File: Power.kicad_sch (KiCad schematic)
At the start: 31 parts, among them J1 S2B-PH-K-S, Q2 SSM3J35MFV, Q3 SSM3K16FV, U6 TPS629203DRL, U9 TPS629206DRLR

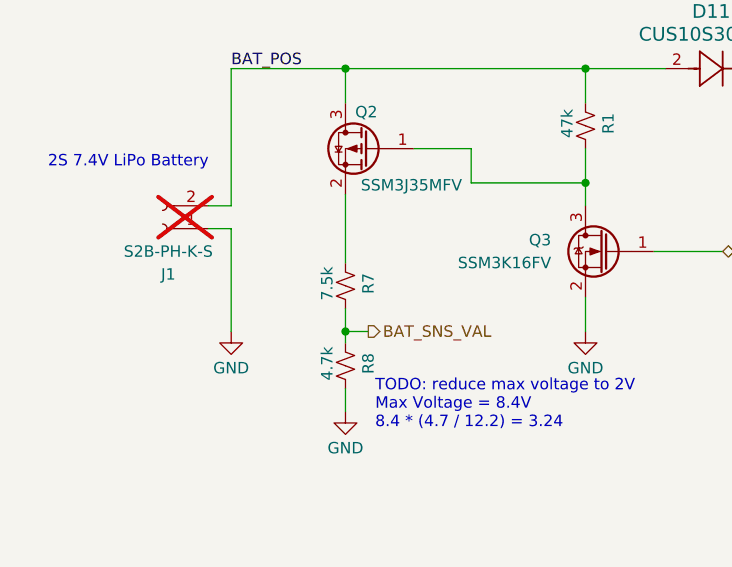
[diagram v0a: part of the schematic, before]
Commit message: rev2 precheck DRC clean
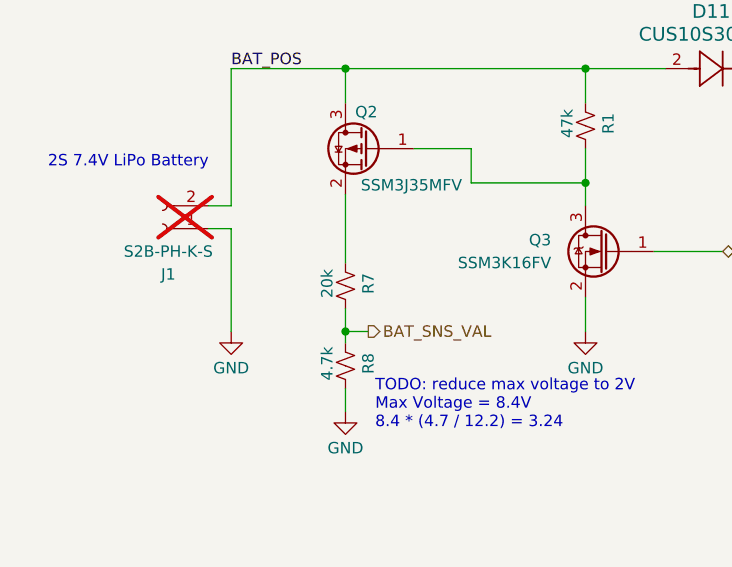
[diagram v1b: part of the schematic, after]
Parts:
- R7: value 7.5k -> 20k; Distributor Prt # 311-7.50KLRCT-ND -> 311-20.0KLRCT-ND; Manuf Prt # RC0402FR-077K5L -> RC0402FR-0720KL
- TP11, TP14, TP15, TP7, TP8: footprint TestPoint:TestPoint_Pad_D1.0mm -> TestPoint:TestPoint_THTPad_1.0x1.0mm_Drill0.5mm
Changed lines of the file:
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@@
 			)
 		)
-		(property "Footprint" "TestPoint:TestPoint_Pad_D1.0mm"
+		(property "Footprint" "TestPoint:TestPoint_THTPad_1.0x1.0mm_Drill0.5mm"
 			(at 105.41 81.28 0)
 			(effects
@@
 			)
 		)
-		(property "Footprint" "TestPoint:TestPoint_Pad_D1.0mm"
+		(property "Footprint" "TestPoint:TestPoint_THTPad_1.0x1.0mm_Drill0.5mm"
 			(at 267.97 41.91 0)
 			(effects
@@
 			)
 		)
-		(property "Footprint" "TestPoint:TestPoint_Pad_D1.0mm"
+		(property "Footprint" "TestPoint:TestPoint_THTPad_1.0x1.0mm_Drill0.5mm"
 			(at 204.47 107.95 0)
 			(effects
@@
 			)
 		)
-		(property "Footprint" "TestPoint:TestPoint_Pad_D1.0mm"
+		(property "Footprint" "TestPoint:TestPoint_THTPad_1.0x1.0mm_Drill0.5mm"
 			(at 96.52 81.28 0)
 			(effects
@@
 			)
 		)
-		(property "Footprint" "TestPoint:TestPoint_Pad_D1.0mm"
+		(property "Footprint" "TestPoint:TestPoint_THTPad_1.0x1.0mm_Drill0.5mm"
 			(at 248.92 97.79 0)
 			(effects
@@
 			)
 		)
-		(property "Value" "7.5k"
+		(property "Value" "20k"
 			(at 51.308 103.886 90)
 			(effects
@@
 			)
 		)
-		(property "Description" "RES 7.5K OHM 1% 1/16W 0402"
+		(property "Description" "RES 20K OHM 1% 1/16W 0402"
 			(at 53.34 104.14 0)
 			(effects
@@
 			)
 		)
-		(property "Distributor Prt #" "311-7.50KLRCT-ND"
+		(property "Distributor Prt #" "311-20.0KLRCT-ND"
 			(at 53.34 104.14 0)
 			(effects
@@
 			)
 		)
-		(property "Manuf Prt #" "RC0402FR-077K5L"
+		(property "Manuf Prt #" "RC0402FR-0720KL"
 			(at 53.34 104.14 0)
 			(effects

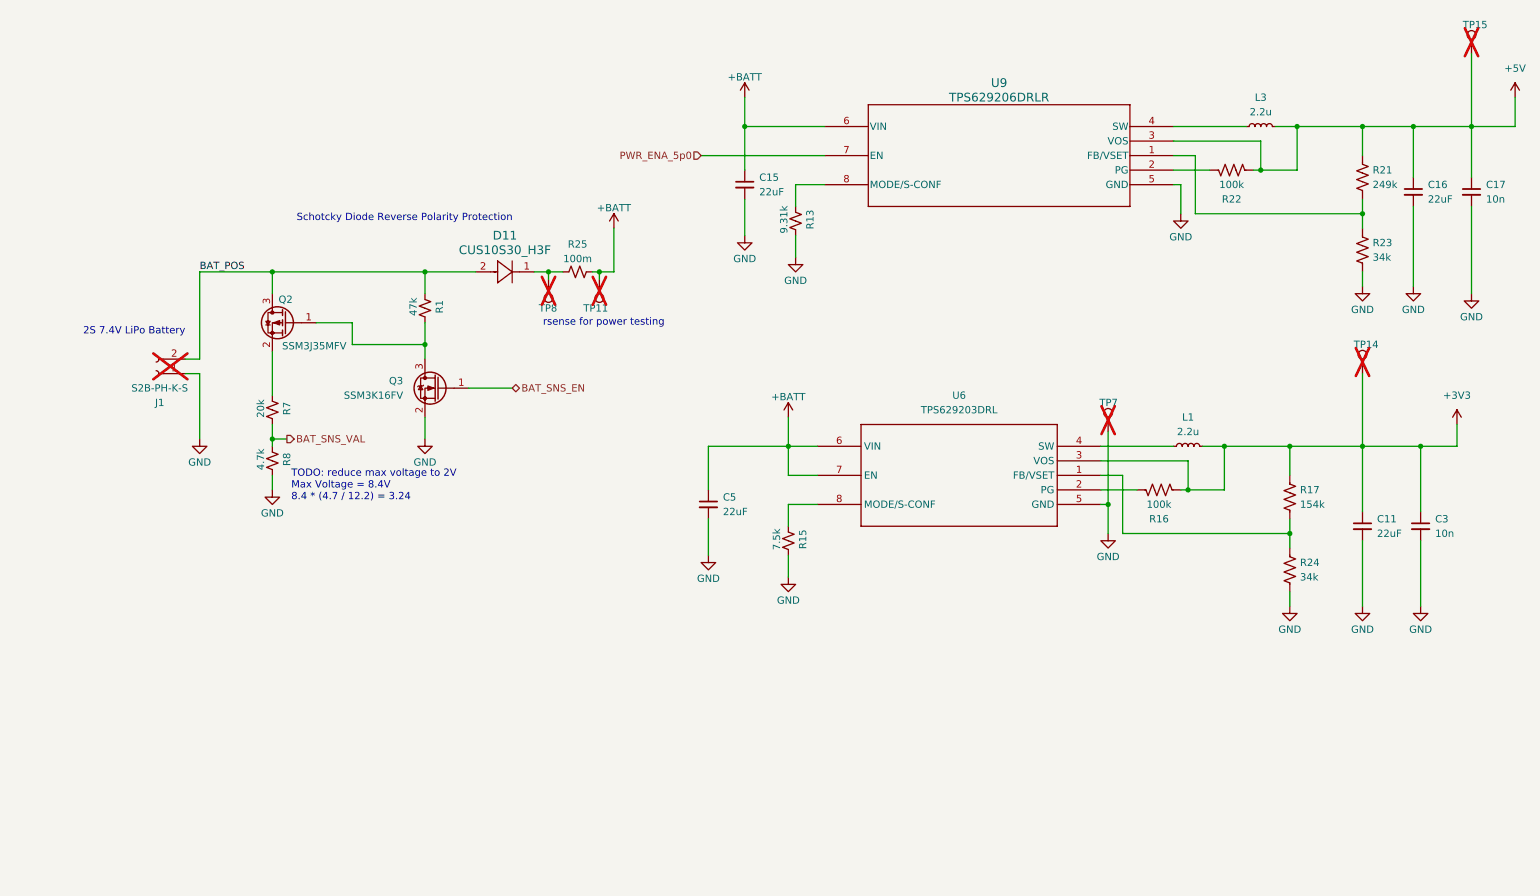
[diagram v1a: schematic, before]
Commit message: updated schematic for pwr savings
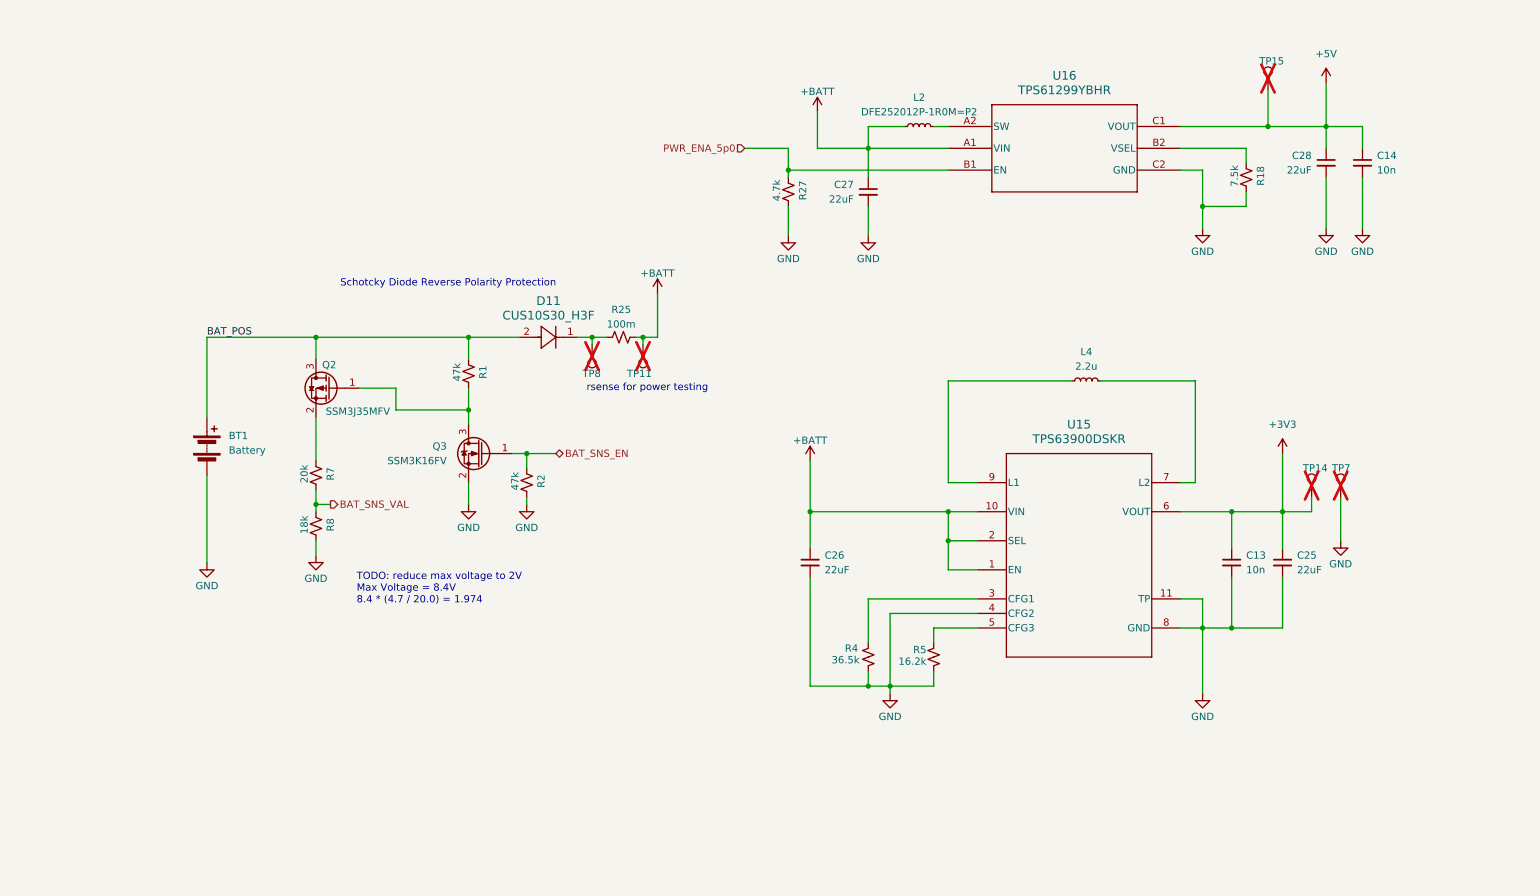
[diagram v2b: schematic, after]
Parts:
- removed C11, C15, C16, C5: 22uF, Capacitor_SMD:C_0805_2012Metric, symbol Device:C_Small
- removed C17, C3: 10n, Capacitor_SMD:C_0201_0603Metric, symbol Device:C_Small
- removed J1: S2B-PH-K-S, SproutSenseFootprints:CONN_S2B-PH-K-S_JST, symbol Connector:Conn_01x02_Socket
- removed L1, L3: 2.2u, SproutSenseFootprints:IND_VLS3012CX-2R2M-1, symbol Device:L_Small
- removed R13: 9.31k, Resistor_SMD:R_0402_1005Metric, symbol Device:R_Small_US
- removed R15: 7.5k, Resistor_SMD:R_0402_1005Metric, symbol Device:R_Small_US
- removed R16, R22: 100k, Resistor_SMD:R_0402_1005Metric, symbol Device:R_US
- removed R17: 154k, Resistor_SMD:R_0402_1005Metric, symbol Device:R_US
- removed R21: 249k, Resistor_SMD:R_0402_1005Metric, symbol Device:R_US
- removed R23, R24: 34k, Resistor_SMD:R_0402_1005Metric, symbol Device:R_US
- removed U6: TPS629203DRL, SproutSenseFootprints:SOT5X3-8_DRL_TEX, symbol SproutSense:TPS629203DRL
- removed U9: TPS629206DRLR, SproutSenseFootprints:SOT5X3-8_DRL_TEX, symbol SproutSense:TPS629206DRLR
- added BT1: Battery, SproutSenseFootprints:BatteryHolder_21700, symbol Device:Battery
- added C13, C14: 10n, Capacitor_SMD:C_0201_0603Metric, symbol Device:C_Small
- added C25, C26, C27, C28: 22uF, Capacitor_SMD:C_0805_2012Metric, symbol Device:C_Small
- added L2: DFE252012P-1R0M=P2, SproutSenseFootprints:DFE252012P-1R0M=P2, symbol Device:L_Small
- added L4: 2.2u, SproutSenseFootprints:IND_VLS3012CX-2R2M-1, symbol Device:L_Small
- added R18: 7.5k, Resistor_SMD:R_0402_1005Metric, symbol Device:R_Small_US
- added R2: 47k, Resistor_SMD:R_0402_1005Metric, symbol Device:R_Small_US
- added R27: 4.7k, Resistor_SMD:R_0402_1005Metric, symbol Device:R_Small_US
- added R4: 36.5k, Resistor_SMD:R_0805_2012Metric, symbol Device:R_Small_US
- added R5: 16.2k, Resistor_SMD:R_0805_2012Metric, symbol Device:R_Small_US
- added U15: TPS63900DSKR, SproutSenseFootprints:DSK0010A, symbol SproutSense:TPS63900DSKR
- added U16: TPS61299YBHR, SproutSenseFootprints:DSBGA6_YBH_TEX, symbol SproutSense:TPS61299YBHR
- R8: value 4.7k -> 18k; Distributor Prt # 311-4.7KJRCT-ND -> A130370TR-ND; Manuf Prt # RC0402JR-074K7L -> CRGP0402F18K
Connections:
- net +3V3: now also C13.1, C25.1, U15.6 (VOUT)
- net +5V: now also C14.1, C28.1, U16.C1 (VOUT)
- net +BATT: now also C26.1, C27.1, L2.1, U15.1 (EN), U15.10 (VIN), U15.2 (SEL), U16.A1 (VIN)
- net BAT_POS: now also BT1.1 (+)
- net BAT_SNS_EN: now also R2.2
- net GND: now also BT1.2 (-), C13.2, C14.2, C25.2, C26.2, C27.2, C28.2, R18.1, R2.1, R27.1, R4.2, R5.2, U15.11 (TP), U15.4 (CFG2), U15.8 (GND), U16.C2 (GND)
- net PWR_ENA_5p0: now also R27.2, U16.B1 (EN)
- new net: R4.1, U15.3 (CFG1)
- new net: L2.2, U16.A2 (SW)
- new net: R5.1, U15.5 (CFG3)
- new net: L4.2, U15.7 (L2)
- new net: L4.1, U15.9 (L1)
- new net: R18.2, U16.B2 (VSEL)
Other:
- note added: "TODO: reduce max voltage to 2V Max Voltage = 8.4V 8.4 * (4.7 / 20.0) = 1.974"
- note removed: "2S 7.4V LiPo Battery"
- note removed: "TODO: reduce max voltage to 2V Max Voltage = 8.4V 8.4 * (4.7 / 12.2) = 3.24"
- title: SproutSyncProto-A-01 -> SproutSyncProto-A-02
- moved on the sheet: D11, Q2, Q3, R1, R25, R7, R8, TP11, TP14, TP7, TP8

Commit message: updated pcb for pwr savings
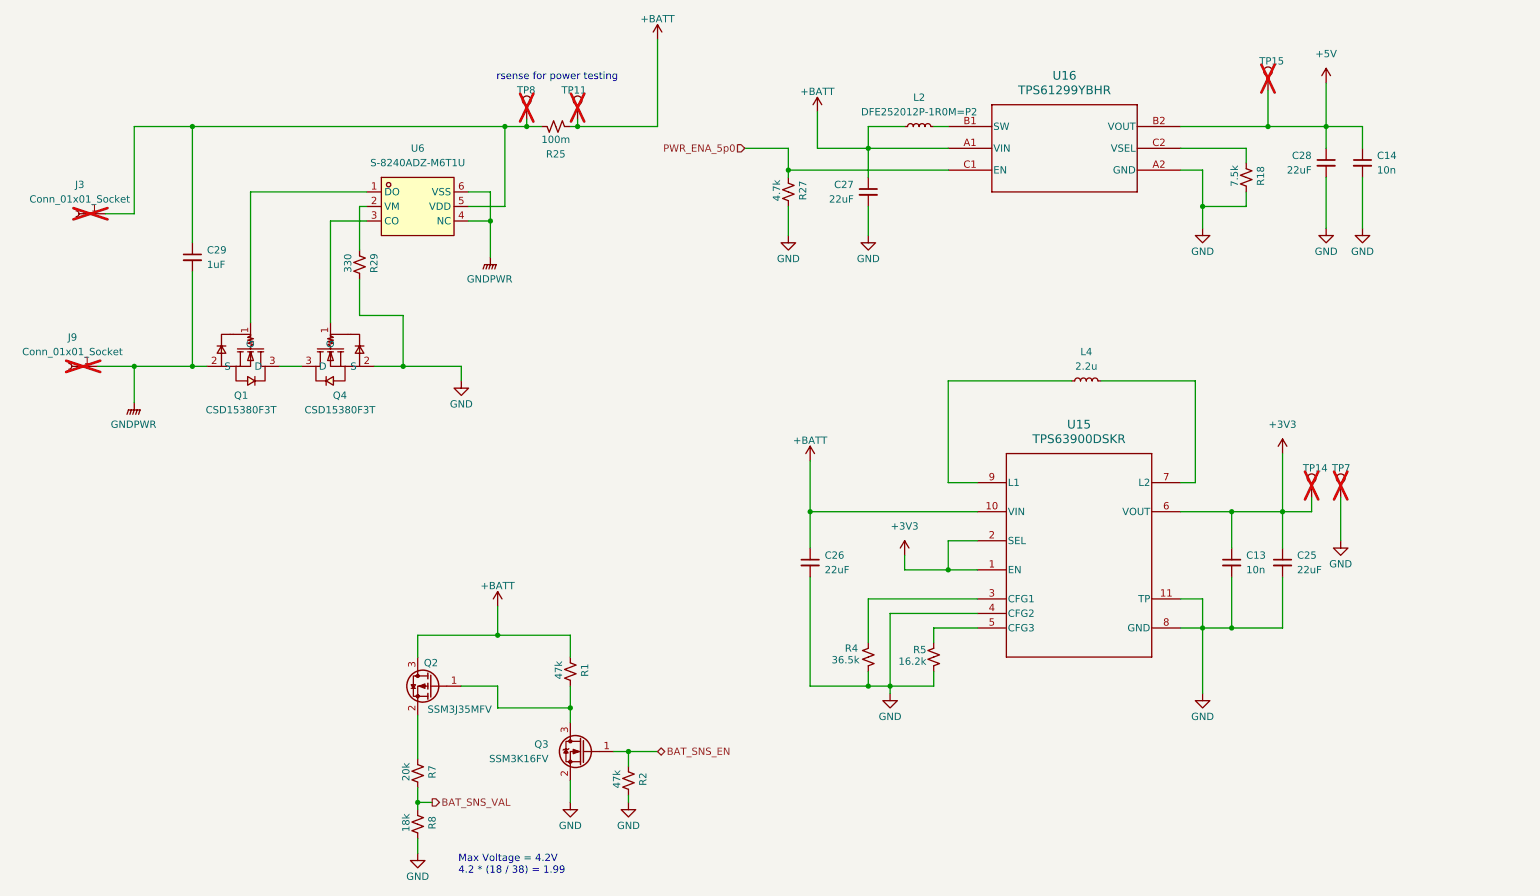
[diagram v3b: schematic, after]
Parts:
- removed BT1: Battery, SproutSenseFootprints:BatteryHolder_21700, symbol Device:Battery
- removed D11: CUS10S30_H3F, SproutSenseFootprints:USC_TOS, symbol SproutSense:CUS10S30_H3F
- added C29: 1uF, Capacitor_SMD:C_0402_1005Metric, symbol Device:C_Small
- added J3, J9: Conn_01x01_Socket, SproutSenseFootprints:BAT_247, symbol Connector:Conn_01x01_Socket
- added Q1, Q4: CSD15380F3T, EasyEDA:PICOSTAR-3_L0.7-W0.6-P0.35-TL, symbol EasyEDA:CSD15380F3T
- added R29: 330, Resistor_SMD:R_0402_1005Metric, symbol Device:R_Small_US
- added U6: S-8240ADZ-M6T1U, EasyEDA:SOT-23-6_L2.9-W1.6-P0.95-LS2.8-TL, symbol EasyEDA:S-8240ADZ-M6T1U
- C25, C26, C27, C28: footprint Capacitor_SMD:C_0805_2012Metric -> Capacitor_SMD:C_0402_1005Metric; Distributor Prt # 490-GRM21BZ71A226ME15LCT-ND -> 490-GRM158R60J226ME01DCT-ND; Manuf Prt # GRM21BZ71A226ME15L -> GRM158R60J226ME01D
- U16: footprint SproutSenseFootprints:DSBGA6_YBH_TEX -> DSBGA6_YBH_TEX
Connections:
- net BAT_POS is gone; now on net +BATT: Q2.3 (D), R1.2
- net +3V3: now also U15.1 (EN), U15.2 (SEL)
- net +5V: now also U16.B2 (VOUT); no longer U16.C1 (VOUT)
- net +BATT: no longer U15.1 (EN), U15.2 (SEL)
- net GND: now also U16.A2 (GND), Q4.2 (S), R29.1; no longer U16.C2 (GND)
- net PWR_ENA_5p0: now also U16.C1 (EN); no longer U16.B1 (EN)
- net at L2.2: now also U16.B1 (SW); no longer U16.A2 (SW)
- net at R18.2: now also U16.C2 (VSEL); no longer U16.B2 (VSEL)
- net at R25.1, TP8.1: now also C29.1, J3.1 (Pin_1), U6.5 (VDD)
- new net: Q1.1 (G), U6.1 (DO)
- new net: R29.2, U6.2 (VM)
- new net: Q4.1 (G), U6.3 (CO)
- new net: Q1.3 (D), Q4.3 (D)
- new net GNDPWR: C29.2, J9.1 (Pin_1), Q1.2 (S), U6.4 (NC), U6.6 (VSS)
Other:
- note added: "Max Voltage = 4.2V 4.2 * (18 / 38) = 1.99"
- note removed: "Schotcky Diode Reverse Polarity Protection"
- note removed: "TODO: reduce max voltage to 2V Max Voltage = 8.4V 8.4 * (4.7 / 20.0) = 1.974"
- title: SproutSyncProto-A-02 -> SproutSyncProto-A-04
- moved on the sheet: Q2, Q3, R1, R2, R25, R7, R8, TP11, TP8
